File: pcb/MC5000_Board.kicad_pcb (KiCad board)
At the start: 2 copper layers, 100 x 80.5 mm, 99 parts, among them J1 USB_B_Micro, J17 Conn_01x04_Female, J20 Conn_01x04_Female, J24 Conn_01x04_Female, J25 Conn_01x05_Female, Q1 S9013, SW1 SW_MEC_5E, SW2 SW_MEC_5E, U1 PFS173-S08, U2 PFS173-S08, U3 PFS173-S08, U4 PFS173-S08, U5 CH340E, U8 PCA9555PW

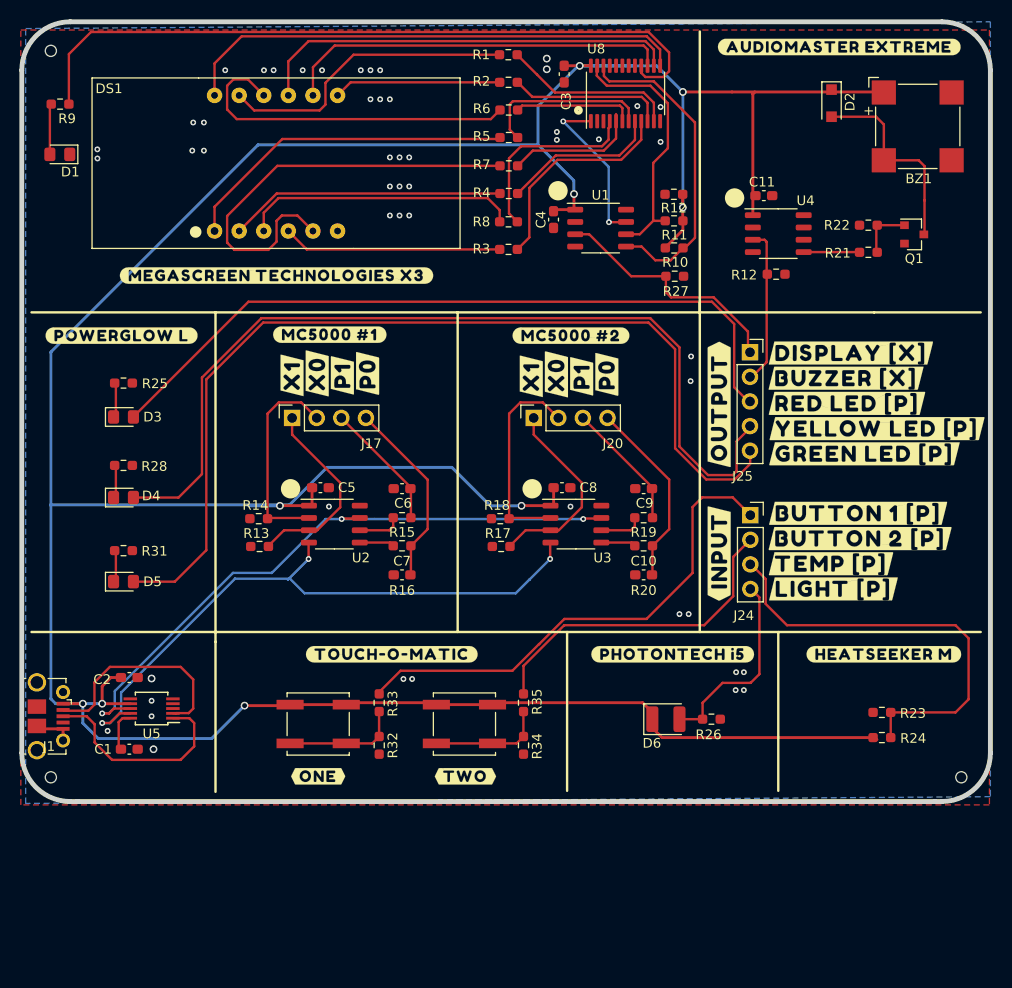
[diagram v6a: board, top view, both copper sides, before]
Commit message: Fixed USB footprint
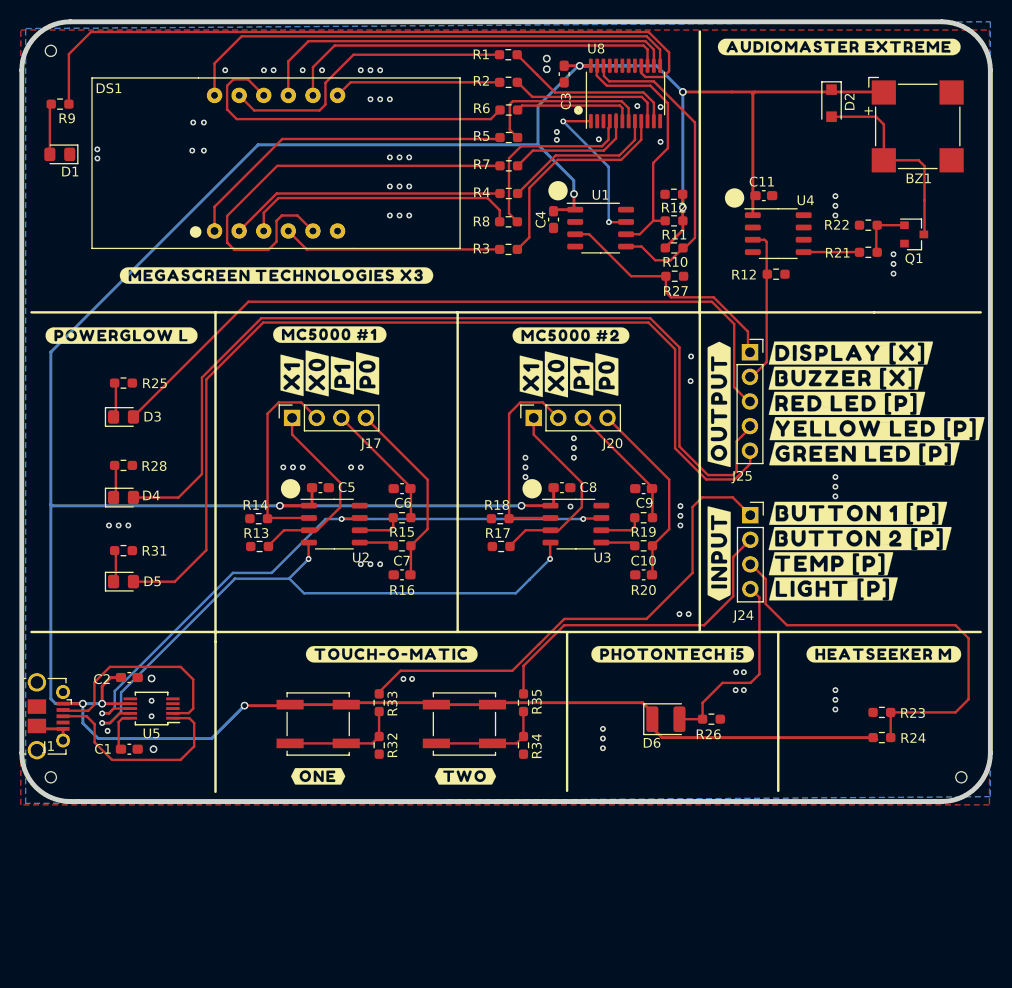
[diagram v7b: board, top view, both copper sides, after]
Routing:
- net VCC: track 356.7 -> 350.2 mm
- net GND: vias 51 -> 85

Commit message: One PCB to rule them all
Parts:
- removed the REF** at (52.5, 42.5)
- removed the REF** at (146.5, 117.3)
- removed the REF** at (53.0, 117.9)
- added ?: , buzzard_labels, F.Cu at (91.9, 136.2)
- added ?: , buzzard_labels, F.Cu at (108.0, 136.2)
- added ?: , buzzard_labels, F.Cu at (75.8, 136.2)
- added ?: , buzzard_labels, F.Cu at (60.1, 136.2)
- added J14: Conn_01x04_Female, LCSC_parts:PinSocket_1x04_P2.54mm_Vertical_centered, F.Cu at (106.7, 59.9)
- added J15: Conn_01x04_Female, LCSC_parts:PinSocket_1x04_P2.54mm_Vertical_centered, F.Cu at (114.3, 59.9)
- added J16: Conn_01x04_Female, LCSC_parts:PinSocket_1x04_P2.54mm_Vertical_centered, F.Cu at (77.6, 93.7)
- added J18: Conn_01x04_Female, LCSC_parts:PinSocket_1x04_P2.54mm_Vertical_centered, F.Cu at (85.2, 93.7)
- added J19: Conn_01x04_Female, LCSC_parts:PinSocket_1x04_P2.54mm_Vertical_centered, F.Cu at (102.6, 93.7)
- added J2: Conn_01x04_Male, LCSC_parts:PinHeader_1x04_P2.54mm_Vertical_centered, B.Cu at (104.2, 129.8)
- added J21: Conn_01x04_Female, LCSC_parts:PinSocket_1x04_P2.54mm_Vertical_centered, F.Cu at (110.2, 93.7)
- added J22: Conn_01x04_Female, LCSC_parts:PinSocket_1x04_P2.54mm_Vertical_centered, F.Cu at (124.7, 59.9)
- added J23: Conn_01x04_Female, LCSC_parts:PinSocket_1x04_P2.54mm_Vertical_centered, F.Cu at (132.3, 59.9)
- added J3: Conn_01x04_Male, LCSC_parts:PinHeader_1x04_P2.54mm_Vertical_centered, B.Cu at (111.8, 129.8)
- added J4: Conn_01x04_Male, LCSC_parts:PinHeader_1x04_P2.54mm_Vertical_centered, B.Cu at (56.2, 129.8)
- added J5: Conn_01x04_Male, LCSC_parts:PinHeader_1x04_P2.54mm_Vertical_centered, B.Cu at (63.8, 129.8)
- added J6: Conn_01x04_Male, LCSC_parts:PinHeader_1x04_P2.54mm_Vertical_centered, B.Cu at (72.2, 129.8)
- added J7: Conn_01x04_Male, LCSC_parts:PinHeader_1x04_P2.54mm_Vertical_centered, B.Cu at (79.8, 129.8)
- added J8: Conn_01x04_Male, LCSC_parts:PinHeader_1x04_P2.54mm_Vertical_centered, B.Cu at (88.2, 129.8)
- added J9: Conn_01x04_Male, LCSC_parts:PinHeader_1x04_P2.54mm_Vertical_centered, B.Cu at (95.8, 129.8)
- added REF**: JLC_assembly_hole, LCSC_parts:JLC_assembly_hole, F.Cu at (53.0, 43.0)
- added REF**: 2mm, Holes:2mm, F.Cu at (61.5, 121.5)
- added REF**: 2mm, Holes:2mm, F.Cu at (58.5, 121.5)
- added REF**: JLC_assembly_hole, LCSC_parts:JLC_assembly_hole, F.Cu at (53.0, 118.0)
- added REF**: JLC_assembly_hole, LCSC_parts:JLC_assembly_hole, F.Cu at (147.0, 118.0)
- added REF**: 2mm, Holes:2mm, F.Cu at (109.5, 121.5)
- added REF**: 2mm, Holes:2mm, F.Cu at (106.5, 121.5)
- added REF**: 2mm, Holes:2mm, F.Cu at (93.5, 121.5)
- added REF**: 2mm, Holes:2mm, F.Cu at (90.5, 121.5)
- added REF**: 2mm, Holes:2mm, F.Cu at (77.5, 121.5)
- added REF**: 2mm, Holes:2mm, F.Cu at (74.5, 121.5)
- D6: footprint LED_SMD:LED_1210_3225Metric -> LCSC_parts:LED_1210_3225Metric_Pad1.42x2.65mm_rotated
- U1, U2, U3, U4: footprint Package_SO:SOP-8_3.9x4.9mm_P1.27mm -> LCSC_parts:SOP-8_3.9x4.9mm_P1.27mm_rotated
- U5: footprint Package_SO:MSOP-10_3x3mm_P0.5mm -> LCSC_parts:MSOP-10_3x3mm_P0.5mm_rotated
- U8: footprint Package_SO:TSSOP-24_4.4x7.8mm_P0.65mm -> LCSC_parts:TSSOP-24_4.4x7.8mm_P0.65mm_rotated
- moved U4 77.1 mm to (92.0, 130.0)
- moved U1 68.7 mm to (108.0, 130.0)
- moved U3 49.3 mm to (76.0, 130.0)
- moved U2 44.2 mm to (60.0, 130.0)
- moved R14 7.18 mm to (81.5, 92.7), turned to 180 degrees
- moved R18 7.16 mm to (106.4, 92.8), turned to 180 degrees
- moved R12 7.10 mm to (128.6, 59.0)
- moved R13 7.10 mm to (81.5, 95.6), turned to 0 degrees
- moved C4 7.09 mm to (110.5, 56.1), turned to 180 degrees
- moved R17 7.08 mm to (106.4, 95.7), turned to 0 degrees
- moved R11 6.87 mm to (110.5, 61.5), turned to 180 degrees
- moved R27 6.87 mm to (110.6, 67.2)
- moved R10 6.87 mm to (110.5, 64.2)
- moved R12 6.85 mm to (110.5, 58.8), turned to 180 degrees
- moved C11 2.72 mm to (128.6, 56.1)
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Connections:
- C4 pad 1: VCC -> GND
- C4 pad 2: GND -> VCC
- D6 pad 1: VCC -> LIGHT_SENSOR
- D6 pad 2: LIGHT_SENSOR -> VCC
- J17 pad 1: Net-(J17-Pad1) -> Net-(J16-Pad3)
- J17 pad 2: Net-(J17-Pad2) -> Net-(J16-Pad2)
- J20 pad 1: Net-(J20-Pad1) -> Net-(J19-Pad3)
- J20 pad 2: Net-(J20-Pad2) -> Net-(J19-Pad2)
- R10 pad 2: Net-(R10-Pad2) -> Net-(J15-Pad1)
- R11 pad 1: Net-(R11-Pad1) -> Net-(J15-Pad2)
- R13 pad 1: Net-(J17-Pad1) -> Net-(J16-Pad3)
- R14 pad 2: Net-(J17-Pad2) -> Net-(J16-Pad2)
- R15 pad 1: Net-(R15-Pad1) -> Net-(J18-Pad2)
- R16 pad 2: Net-(R16-Pad2) -> Net-(J18-Pad1)
- R17 pad 1: Net-(J20-Pad1) -> Net-(J19-Pad3)
- R18 pad 2: Net-(J20-Pad2) -> Net-(J19-Pad2)
- R19 pad 1: Net-(R19-Pad1) -> Net-(J21-Pad2)
- R20 pad 2: Net-(R20-Pad2) -> Net-(J21-Pad1)
- R21 pad 2: Net-(R21-Pad2) -> Net-(J23-Pad1)
- U1 pad 1: VCC -> Net-(J2-Pad1)
- U1 pad 3: DISPLAY -> Net-(J2-Pad3)
- U1 pad 5: Net-(R10-Pad2) -> Net-(J3-Pad1)
- U1 pad 6: Net-(R11-Pad1) -> Net-(J3-Pad2)
- U1 pad 7: Net-(U1-Pad7) -> Net-(J3-Pad3)
- U1 pad 8: GND -> Net-(J3-Pad4)
- U2 pad 1: VCC -> Net-(J4-Pad1)
- U2 pad 2: Net-(J17-Pad2) -> Net-(J4-Pad2)
- U2 pad 3: Net-(J17-Pad1) -> Net-(J4-Pad3)
- U2 pad 4: RXD -> Net-(J4-Pad4)
- U2 pad 5: Net-(R16-Pad2) -> Net-(J5-Pad1)
- U2 pad 6: Net-(R15-Pad1) -> Net-(J5-Pad2)
- U2 pad 7: TXD -> Net-(J5-Pad3)
- U2 pad 8: GND -> Net-(J5-Pad4)
- U3 pad 1: VCC -> Net-(J6-Pad1)
- U3 pad 2: Net-(J20-Pad2) -> Net-(J6-Pad2)
- U3 pad 3: Net-(J20-Pad1) -> Net-(J6-Pad3)
- U3 pad 4: RXD -> Net-(J6-Pad4)
- U3 pad 5: Net-(R20-Pad2) -> Net-(J7-Pad1)
- U3 pad 6: Net-(R19-Pad1) -> Net-(J7-Pad2)
- U3 pad 7: TXD -> Net-(J7-Pad3)
- U3 pad 8: GND -> Net-(J7-Pad4)
- U4 pad 1: VCC -> Net-(J8-Pad1)
- U4 pad 3: BUZZER -> Net-(J8-Pad3)
- U4 pad 5: Net-(R21-Pad2) -> Net-(J9-Pad1)
- U4 pad 8: GND -> Net-(J9-Pad4)
- U8 pad 1: Net-(U1-Pad7) -> Net-(J15-Pad3)
- U8 pad 22: Net-(R10-Pad2) -> Net-(J15-Pad1)
- U8 pad 23: Net-(R11-Pad1) -> Net-(J15-Pad2)
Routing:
- net Net-(J8-Pad1): track 0.00 -> 35.4 mm
- net Net-(J6-Pad1): track 0.00 -> 35.4 mm
- net Net-(J2-Pad1): track 0.00 -> 35.4 mm
- net Net-(R10-Pad2): track 33.0 -> 0.00 mm
- net Net-(J9-Pad1): track 0.00 -> 33.0 mm, vias 0 -> 3
- net Net-(J7-Pad1): track 0.00 -> 33.0 mm, vias 0 -> 3
- net Net-(J3-Pad1): track 0.00 -> 33.0 mm, vias 0 -> 3
- net Net-(J15-Pad1): track 0.00 -> 29.7 mm
- net Net-(J8-Pad2): track 0.00 -> 29.0 mm, vias 0 -> 3
- net Net-(J6-Pad2): track 0.00 -> 29.0 mm, vias 0 -> 3
- net Net-(J2-Pad2): track 0.00 -> 29.0 mm, vias 0 -> 3
- net Net-(R11-Pad1): track 27.0 -> 0.00 mm
- net Net-(J15-Pad2): track 0.00 -> 26.9 mm
- net Net-(J8-Pad4): track 0.00 -> 24.9 mm
- net Net-(J6-Pad4): track 0.00 -> 24.9 mm
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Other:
- board size 100 x 80.5 mm -> 100 x 97.5 mm
